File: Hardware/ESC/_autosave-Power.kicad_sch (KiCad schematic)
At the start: 41 parts, among them J1 BATT TERM, J24 PWR PROT, J25 PWR 3.3V, Q1 SI7220 NMOS, SW3 PWR, U2 LM2574HVM-3.3, U36 LTC4367

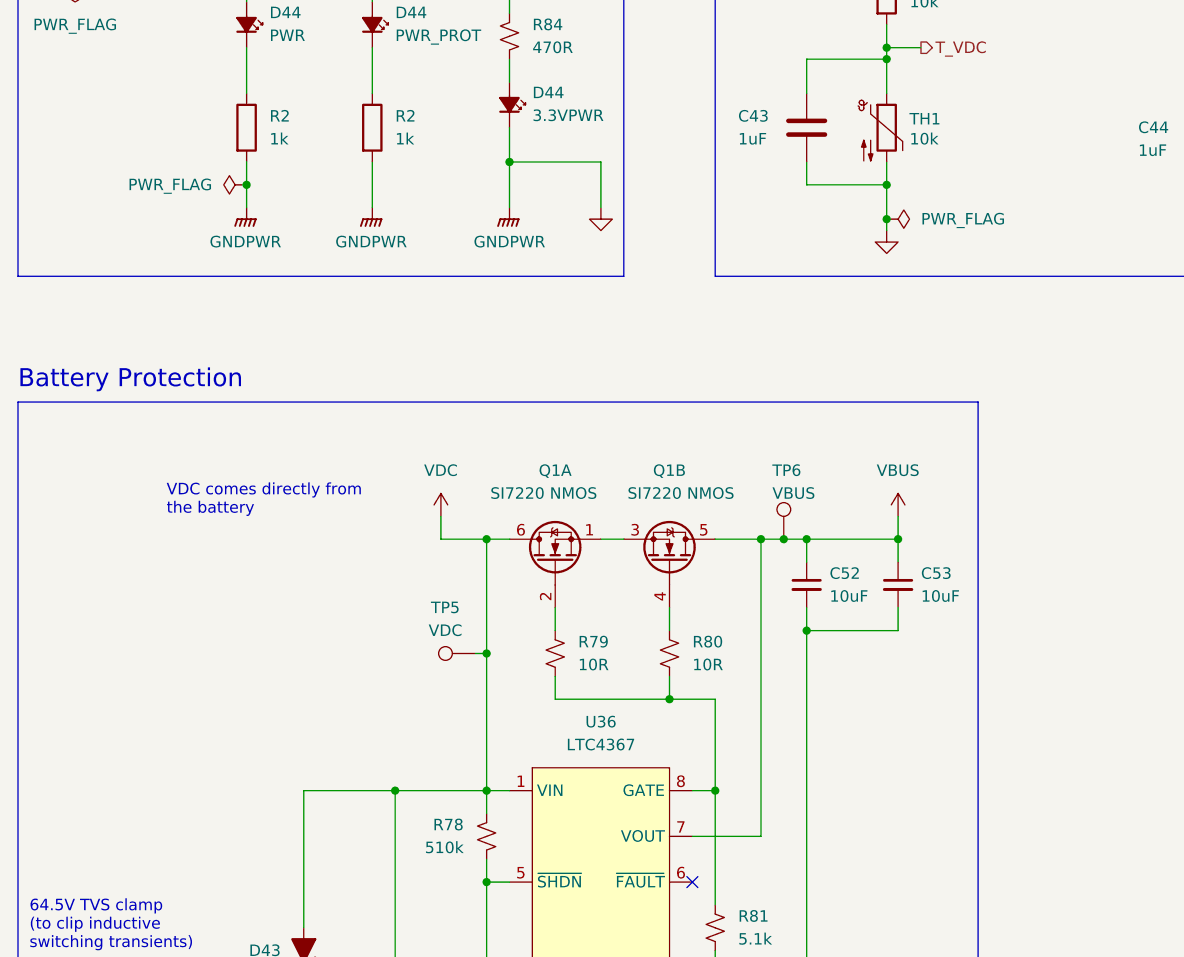
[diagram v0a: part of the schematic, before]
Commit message: Breaking + BEMF ZCD Detector
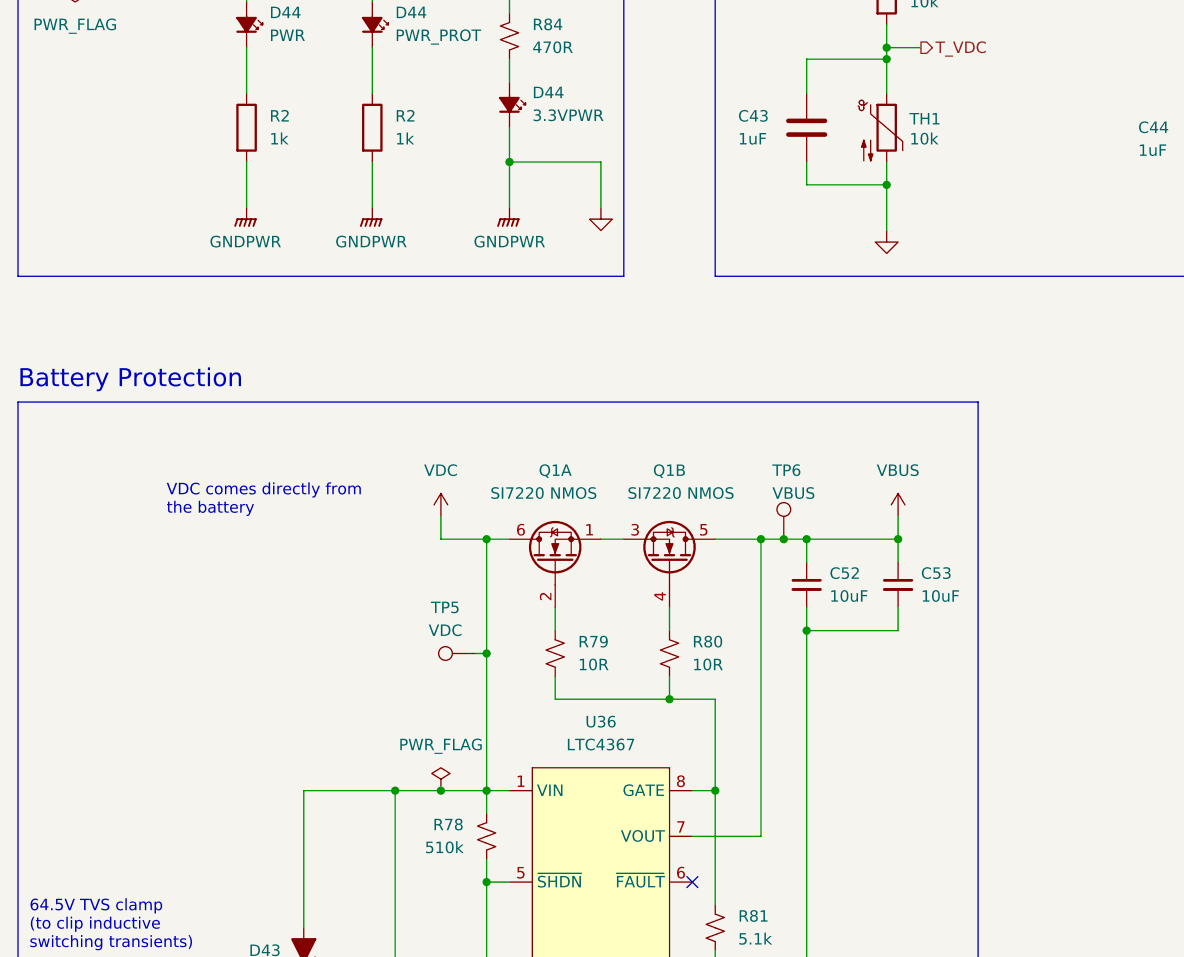
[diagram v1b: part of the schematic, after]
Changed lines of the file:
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@@
 (kicad_sch (version 20230121) (generator eeschema)
   (paper "A4")
-  (junction (at 44.45 54.61) (diameter 0) (color 0 0 0 0)
-  )
   (junction (at 115.57 54.61) (diameter 0) (color 0 0 0 0)
   )
@@
   (junction (at 71.12 132.08) (diameter 0) (color 0 0 0 0)
   )
-  (junction (at 115.57 58.42) (diameter 0) (color 0 0 0 0)
-  )
   (junction (at 160.02 40.64) (diameter 0) (color 0 0 0 0)
   )
@@
   (junction (at 60.96 152.4) (diameter 0) (color 0 0 0 0)
   )
+  (junction (at 160.02 41.91) (diameter 0) (color 0 0 0 0)
+  )
+  (junction (at 60.96 121.92) (diameter 0) (color 0 0 0 0)
+  )
+  (junction (at 106.68 93.98) (diameter 0) (color 0 0 0 0)
+  )
+  (junction (at 68.58 170.18) (diameter 0) (color 0 0 0 0)
+  )
+  (junction (at 218.44 91.44) (diameter 0) (color 0 0 0 0)
+  )
+  (junction (at 264.16 44.45) (diameter 0) (color 0 0 0 0)
+  )
   (junction (at 264.16 36.83) (diameter 0) (color 0 0 0 0)
   )
-  (junction (at 160.02 41.91) (diameter 0) (color 0 0 0 0)
-  )
-  (junction (at 60.96 121.92) (diameter 0) (color 0 0 0 0)
-  )
-  (junction (at 106.68 93.98) (diameter 0) (color 0 0 0 0)
-  )
-  (junction (at 68.58 170.18) (diameter 0) (color 0 0 0 0)
-  )
-  (junction (at 218.44 91.44) (diameter 0) (color 0 0 0 0)
-  )
-  (junction (at 264.16 44.45) (diameter 0) (color 0 0 0 0)
-  )
   (junction (at 71.12 165.1) (diameter 0) (color 0 0 0 0)
   )
@@
   )
   (junction (at 71.12 93.98) (diameter 0) (color 0 0 0 0)
+  )
+  (junction (at 66.04 121.92) (diameter 0) (color 0 0 0 0)
   )
   (junction (at 240.03 44.45) (diameter 0) (color 0 0 0 0)
@@
     (stroke (width 0) (type default))
   )
-  (wire (pts (xy 44.45 54.61) (xy 44.45 57.15))
+  (wire (pts (xy 44.45 52.07) (xy 44.45 57.15))
     (stroke (width 0) (type default))
   )
@@
     (stroke (width 0) (type default))
   )
-  (wire (pts (xy 115.57 54.61) (xy 115.57 58.42))
-    (stroke (width 0) (type default))
-  )
   (wire (pts (xy 71.12 132.08) (xy 71.12 142.24))
     (stroke (width 0) (type default))
@@
     (stroke (width 0) (type default))
   )
-  (wire (pts (xy 44.45 52.07) (xy 44.45 54.61))
-    (stroke (width 0) (type default))
-  )
   (wire (pts (xy 214.63 91.44) (xy 218.44 91.44))
     (stroke (width 0) (type default))
@@
     (stroke (width 0) (type default))
   )
+  (wire (pts (xy 66.04 121.92) (xy 71.12 121.92))
+    (stroke (width 0) (type default))
+  )
   (wire (pts (xy 199.39 91.44) (xy 199.39 97.79))
     (stroke (width 0) (type default))
@@
     (stroke (width 0) (type default))
   )
-  (wire (pts (xy 60.96 121.92) (xy 71.12 121.92))
+  (wire (pts (xy 60.96 121.92) (xy 66.04 121.92))
     (stroke (width 0) (type default))
   )
@@
     (stroke (width 0) (type default))
   )
-  (wire (pts (xy 115.57 58.42) (xy 115.57 59.69))
+  (wire (pts (xy 115.57 54.61) (xy 115.57 59.69))
     (stroke (width 0) (type default))
   )
@@
     )
   )
+  (symbol (lib_id "power:PWR_FLAG") (at 264.16 36.83 270) (unit 1)
+    (in_bom yes) (on_board yes) (dnp no) (fields_autoplaced)
+    (property "Reference" "#FLG05" (at 266.065 36.83 0)
+      (effects (font (size 1.27 1.27)) hide)
+    )
+    (property "Value" "PWR_FLAG" (at 267.97 36.83 90)
+      (effects (font (size 1.27 1.27)) (justify left))
+    )
+    (property "Footprint" "" (at 264.16 36.83 0)
+      (effects (font (size 1.27 1.27)) hide)
+    )
+    (property "Datasheet" "~" (at 264.16 36.83 0)
+      (effects (font (size 1.27 1.27)) hide)
+    )
+    (pin "1")
+    (instances
+      (project "BLDC_ESC"
+        (path "/bd67e774-828f-47d6-928d-7f9ad42d6cab/dac7d52f-093d-43cb-8a30-f6f652ecb1a6"
+          (reference "#FLG05") (unit 1)
+        )
+      )
+    )
+  )
   (symbol (lib_id "Switch:SW_SPST") (at 34.29 31.75 0) (unit 1)
     (in_bom yes) (on_board yes) (dnp no) (fields_autoplaced)
@@
         (path "/bd67e774-828f-47d6-928d-7f9ad42d6cab/dac7d52f-093d-43cb-8a30-f6f652ecb1a6"
           (reference "#PWR032") (unit 1)
-        )
-      )
-    )
-  )
-  (symbol (lib_id "power:PWR_FLAG") (at 44.45 54.61 90) (unit 1)
-    (in_bom yes) (on_board yes) (dnp no) (fields_autoplaced)
-    (property "Reference" "#FLG02" (at 42.545 54.61 0)
-      (effects (font (size 1.27 1.27)) hide)
-    )
-    (property "Value" "PWR_FLAG" (at 40.64 54.61 90)
-      (effects (font (size 1.27 1.27)) (justify left))
-    )
-    (property "Footprint" "" (at 44.45 54.61 0)
-      (effects (font (size 1.27 1.27)) hide)
-    )
-    (property "Datasheet" "~" (at 44.45 54.61 0)
-      (effects (font (size 1.27 1.27)) hide)
-    )
-    (pin "1")
-    (instances
-      (project "BLDC_ESC"
-        (path "/bd67e774-828f-47d6-928d-7f9ad42d6cab/dac7d52f-093d-43cb-8a30-f6f652ecb1a6"
-          (reference "#FLG02") (unit 1)
         )
       )
@@
     )
   )
+  (symbol (lib_id "power:PWR_FLAG") (at 66.04 121.92 0) (unit 1)
+    (in_bom yes) (on_board yes) (dnp no) (fields_autoplaced)
+    (property "Reference" "#FLG04" (at 66.04 120.015 0)
+      (effects (font (size 1.27 1.27)) hide)
+    )
+    (property "Value" "PWR_FLAG" (at 66.04 116.84 0)
+      (effects (font (size 1.27 1.27)))
+    )
+    (property "Footprint" "" (at 66.04 121.92 0)
+      (effects (font (size 1.27 1.27)) hide)
+    )
+    (property "Datasheet" "~" (at 66.04 121.92 0)
+      (effects (font (size 1.27 1.27)) hide)
+    )
+    (pin "1")
+    (instances
+      (project "BLDC_ESC"
+        (path "/bd67e774-828f-47d6-928d-7f9ad42d6cab/dac7d52f-093d-43cb-8a30-f6f652ecb1a6"
+          (reference "#FLG04") (unit 1)
+        )
+      )
+    )
+  )
   (symbol (lib_id "power:GNDPWR") (at 106.68 172.72 0) (unit 1)
     (in_bom yes) (on_board yes) (dnp no)
@@
         (path "/bd67e774-828f-47d6-928d-7f9ad42d6cab/dac7d52f-093d-43cb-8a30-f6f652ecb1a6"
           (reference "C20") (unit 1)
-        )
-      )
-    )
-  )
-  (symbol (lib_id "power:PWR_FLAG") (at 115.57 58.42 270) (unit 1)
-    (in_bom yes) (on_board yes) (dnp no) (fields_autoplaced)
-    (property "Reference" "#FLG03" (at 117.475 58.42 0)
-      (effects (font (size 1.27 1.27)) hide)
-    )
-    (property "Value" "PWR_FLAG" (at 119.38 58.42 90)
-      (effects (font (size 1.27 1.27)) (justify left))
-    )
-    (property "Footprint" "" (at 115.57 58.42 0)
-      (effects (font (size 1.27 1.27)) hide)
-    )
-    (property "Datasheet" "~" (at 115.57 58.42 0)
-      (effects (font (size 1.27 1.27)) hide)
-    )
-    (pin "1")
-    (instances
-      (project "BLDC_ESC"
-        (path "/bd67e774-828f-47d6-928d-7f9ad42d6cab/dac7d52f-093d-43cb-8a30-f6f652ecb1a6"
-          (reference "#FLG03") (unit 1)
         )
       )
@@
         )
       )
-    )
-  )
-  (symbol (lib_id "power:PWR_FLAG") (at 264.16 36.83 270) (unit 1)
-    (in_bom yes) (on_board yes) (dnp no)
-    (property "Reference" "#FLG04" (at 266.065 36.83 0)
-      (effects (font (size 1.27 1.27)) hide)
-    )
-    (property "Value" "PWR_FLAG" (at 267.97 36.83 90)
-      (effects (font (size 1.27 1.27)) (justify left))
-    )
-    (property "Footprint" "" (at 264.16 36.83 0)
-      (effects (font (size 1.27 1.27)) hide)
-    )
-    (property "Datasheet" "~" (at 264.16 36.83 0)
-      (effects (font (size 1.27 1.27)) hide)
-    )
-    (pin "1")
-    (instances
-      (project "BLDC_ESC"
-        (path "/bd67e774-828f-47d6-928d-7f9ad42d6cab/dac7d52f-093d-43cb-8a30-f6f652ecb1a6"
-          (reference "#FLG04") (unit 1)
-        )
-      )
